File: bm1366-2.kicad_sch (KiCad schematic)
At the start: 73 parts, among them U1 25MHz, U15 TLV3544, U16 AP7331, U17 AP7331, U18 BM1366_mode0, U20 BM1366_mode0

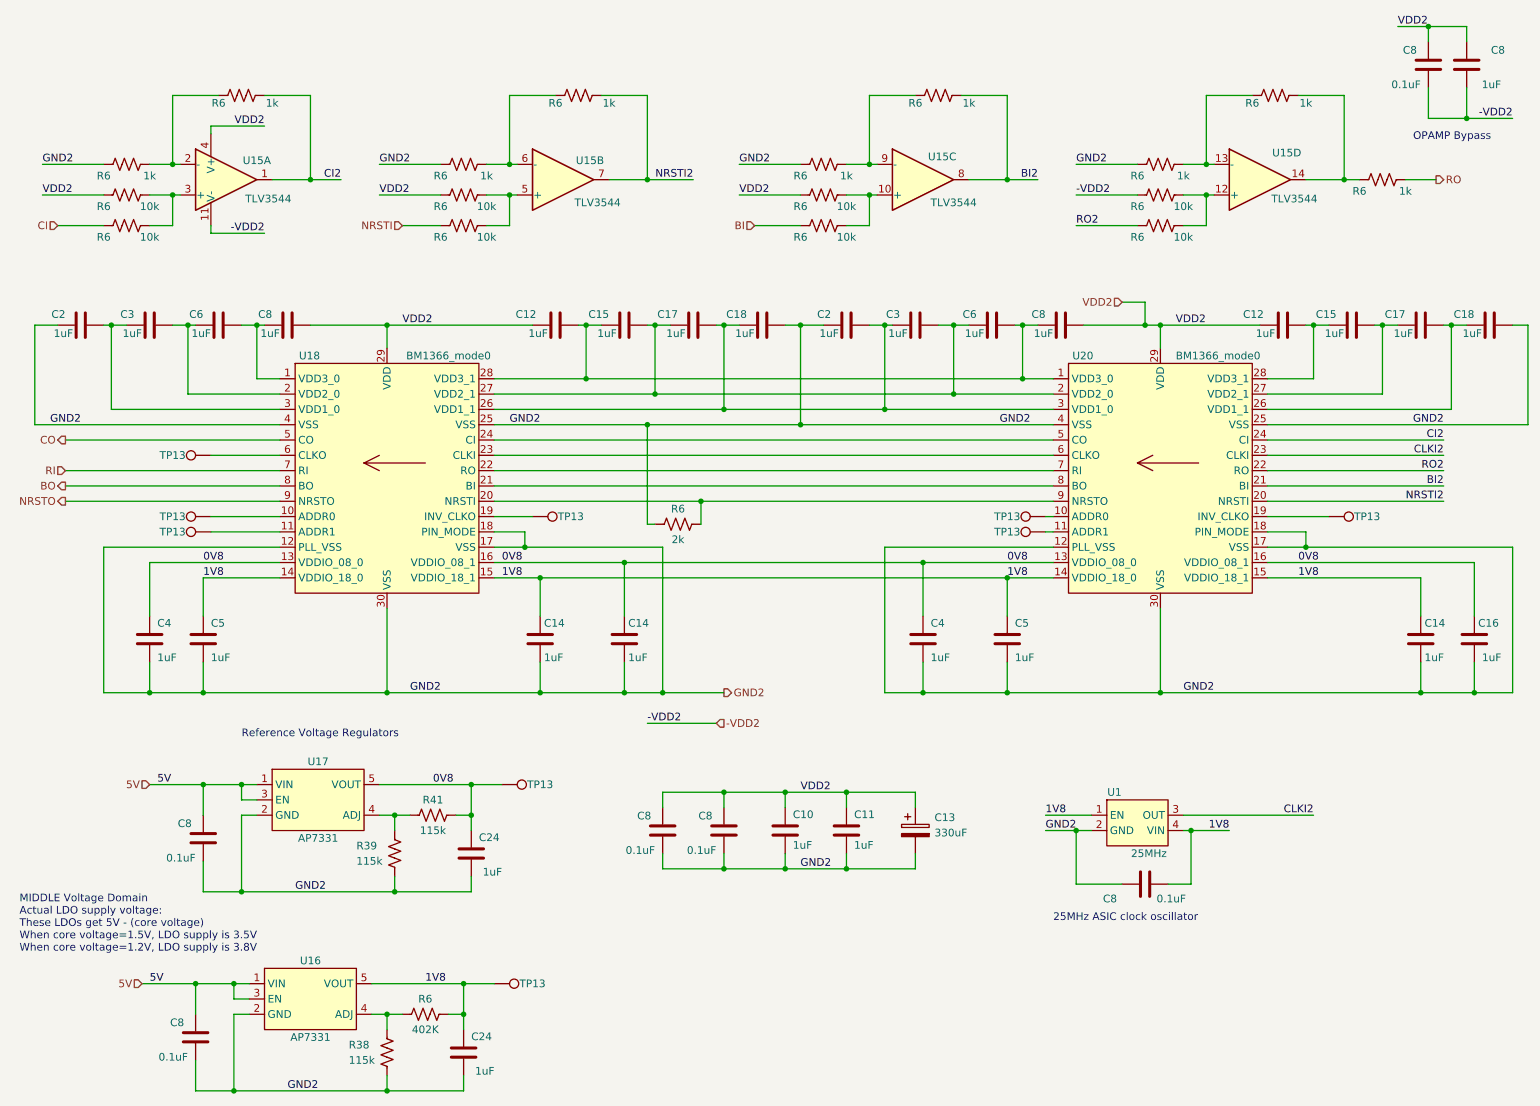
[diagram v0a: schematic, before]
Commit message: finish sch rearrange for BM1368 chain
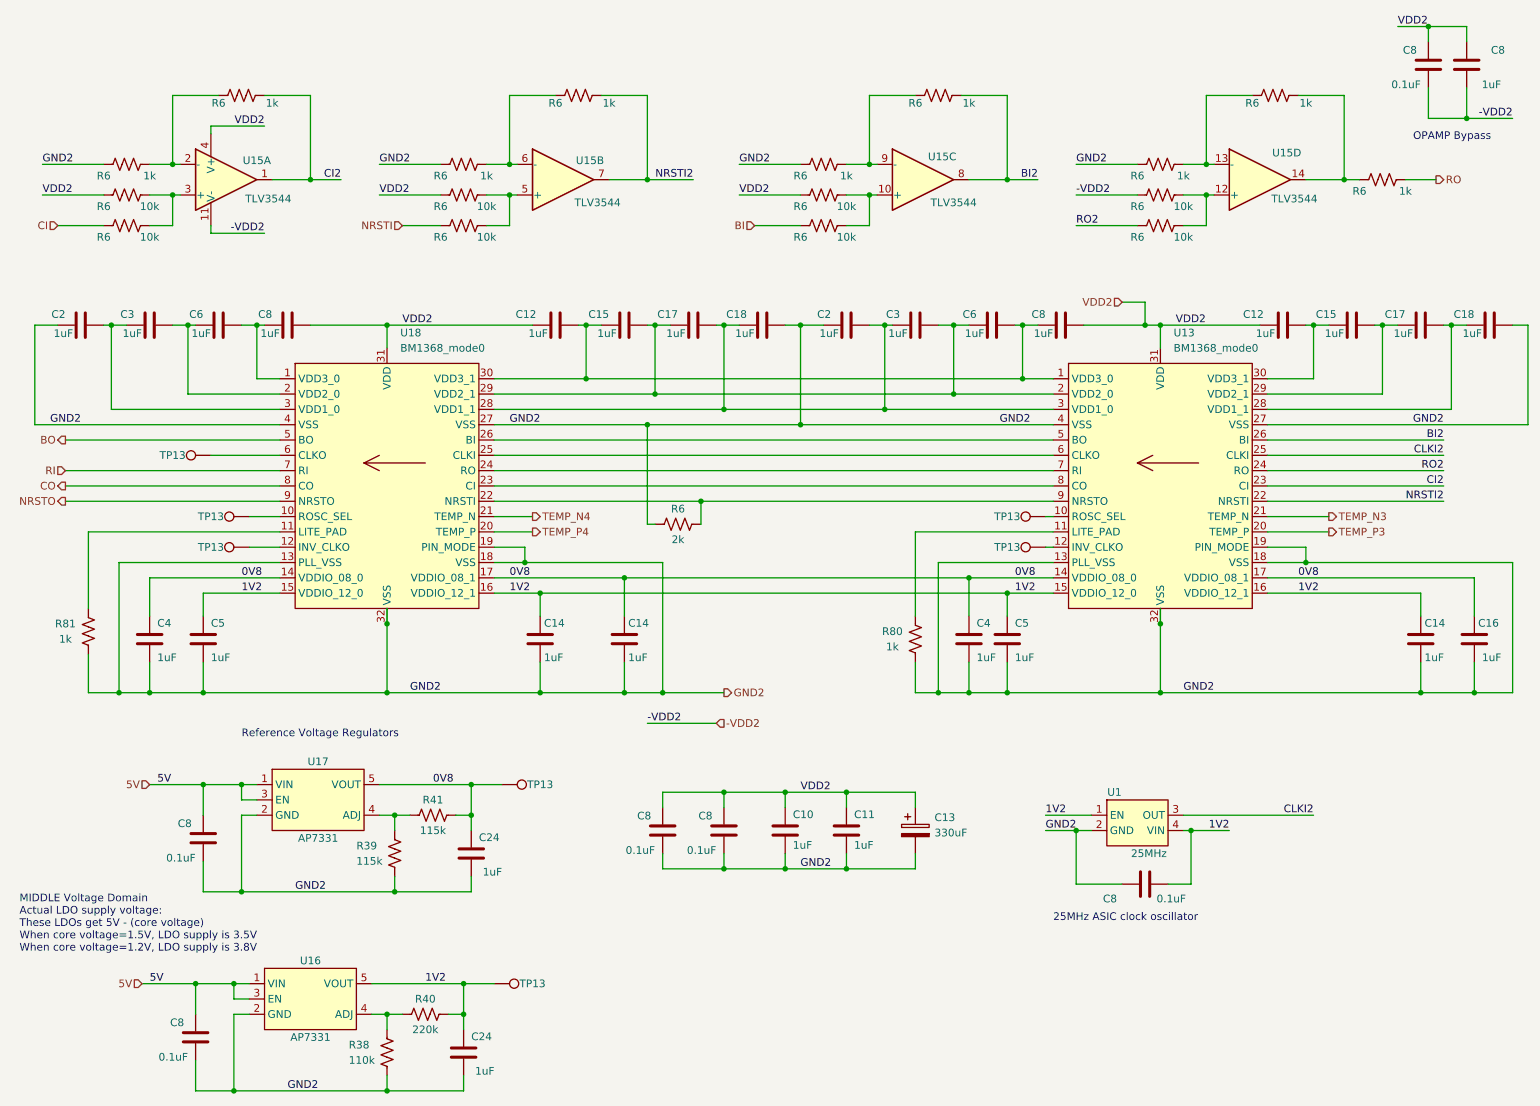
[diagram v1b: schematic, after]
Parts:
- removed R6: 402K, Resistor_SMD:R_0402_1005Metric, symbol Device:R_US
- removed TP13 (x2): TestPoint, TestPoint:TestPoint_Pad_D1.0mm, symbol Connector:TestPoint
- removed U18, U20: BM1366_mode0, bitaxe:BM1366, symbol bitaxe:BM1366_mode0
- added R40: 220k, Resistor_SMD:R_0402_1005Metric, symbol Device:R_US
- added R80, R81: 1k, Resistor_SMD:R_0402_1005Metric, symbol Device:R_US
- added U13, U18: BM1368_mode0, bitaxe:BM1368, symbol bitaxe:BM1368_mode0
- R38: value 115k -> 110k; DK YAG2956CT-ND -> 311-110KLRTR-ND; PARTNO RC0402FR-07115KL -> RC0402FR-07110KL
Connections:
- net 0V8: now also U13.14 (VDDIO_08_0), U13.17 (VDDIO_08_1), U18.14 (VDDIO_08_0), U18.17 (VDDIO_08_1)
- net BI2: now also U13.26 (BI)
- net BO: now also U18.5 (BO)
- net CI2: now also U13.23 (CI)
- net CLKI2: now also U13.25 (CLKI)
- net CO: now also U18.8 (CO)
- net GND2: now also R80.1, R81.1, U13.13 (PLL_VSS), U13.18 (VSS), U13.19 (PIN_MODE), U13.27 (VSS), U13.32 (VSS), U13.4 (VSS), U18.13 (PLL_VSS), U18.18 (VSS), U18.19 (PIN_MODE), U18.27 (VSS), U18.32 (VSS), U18.4 (VSS)
- net NRSTI2: now also U13.22 (NRSTI)
- net NRSTO: now also U18.9 (NRSTO)
- net RI: now also U18.7 (RI)
- net RO2: now also U13.24 (RO)
- net VDD2: now also U13.31 (VDD), U18.31 (VDD)
- net at R6.2: now also U13.9 (NRSTO), U18.22 (NRSTI)
- net at TP13.1: now also U18.10 (ROSC_SEL)
- net at C6.2, C8.1: now also U18.1 (VDD3_0)
- net at C12.2, C15.1, C6.2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: now also U13.1 (VDD3_0), U18.30 (VDD3_1)
- net at C15.2, C17.1, C3.2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: now also U13.2 (VDD2_0), U18.29 (VDD2_1)
- net at TP13.1: now also U18.6 (CLKO)
- net at C17.2, C18.1, C2.2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: now also U13.3 (VDD1_0), U18.28 (VDD1_1)
- net at TP13.1: now also U18.12 (INV_CLKO)
- net at C3.2, C6.1: now also U18.2 (VDD2_0)
- net at C2.2, C3.1: now also U18.3 (VDD1_0)
- net at R38.2, U16.4 (ADJ): now also R40.2
- net at C17.2, C18.1: now also U13.28 (VDD1_1)
- net at TP13.1: now also U13.10 (ROSC_SEL)
- net at TP13.1: now also U13.12 (INV_CLKO)
- net at C12.2, C15.1: now also U13.30 (VDD3_1)
- net at C15.2, C17.1: now also U13.29 (VDD2_1)
- net 1V8 renamed 1V2
- net 1V2: now also R40.1, U13.15 (VDDIO_12_0), U13.16 (VDDIO_12_1), U18.15 (VDDIO_12_0), U18.16 (VDDIO_12_1)
- new net: R80.2, U13.11 (LITE_PAD)
- new net: R81.2, U18.11 (LITE_PAD)
- new net: U13.8 (CO), U18.23 (CI)
- new net: U13.7 (RI), U18.24 (RO)
- new net: U13.6 (CLKO), U18.25 (CLKI)
- new net: U13.5 (BO), U18.26 (BI)
- new net TEMP_N3: U13.21 (TEMP_N)
- new net TEMP_N4: U18.21 (TEMP_N)
- new net TEMP_P3: U13.20 (TEMP_P)
- new net TEMP_P4: U18.20 (TEMP_P)
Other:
- moved on the sheet: C4, TP13

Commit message: Reset to 1V8
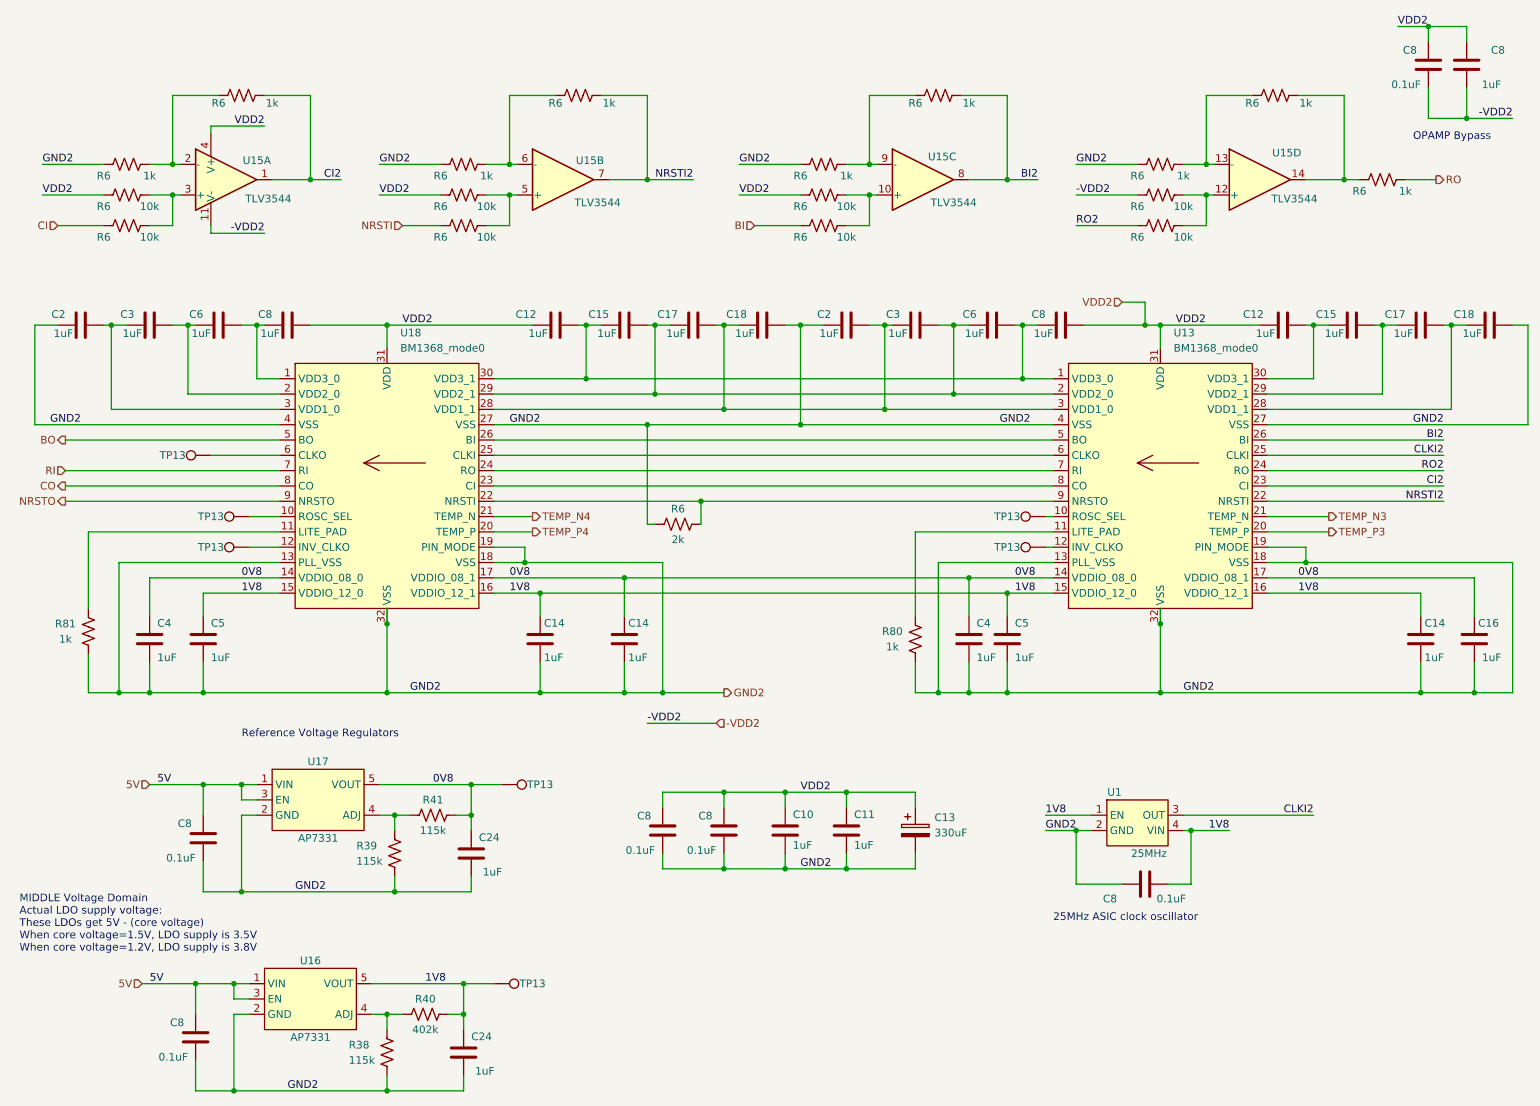
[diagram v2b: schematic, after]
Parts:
- R38: value 110k -> 115k; DK 311-110KLRTR-ND -> YAG2956CT-ND; PARTNO RC0402FR-07110KL -> RC0402FR-07115KL
- R40: value 220k -> 402k; DK 311-220KLRTR-ND -> YAG3151CT-ND; PARTNO RC0402FR-07220KL -> RC0402FR-07402KL
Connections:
- net 1V2 renamed 1V8
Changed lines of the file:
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@@
 		)
 	)
-	(label "1V2"
+	(label "1V8"
 		(at 97.79 111.76 0)
 		(fields_autoplaced yes)
@@
 		)
 	)
-	(label "1V2"
+	(label "1V8"
 		(at 83.82 176.53 0)
 		(fields_autoplaced yes)
@@
 		)
 	)
-	(label "1V2"
+	(label "1V8"
 		(at 217.17 151.13 180)
 		(fields_autoplaced yes)
@@
 		)
 	)
-	(label "1V2"
+	(label "1V8"
 		(at 186.69 148.59 0)
 		(fields_autoplaced yes)
@@
 		)
 	)
-	(label "1V2"
+	(label "1V8"
 		(at 228.6 111.76 0)
 		(fields_autoplaced yes)
@@
 		)
 	)
-	(label "1V2"
+	(label "1V8"
 		(at 53.34 111.76 0)
 		(fields_autoplaced yes)
@@
 		)
 	)
-	(label "1V2"
+	(label "1V8"
 		(at 181.61 111.76 0)
 		(fields_autoplaced yes)
@@
 	)
 	(symbol
+		(lib_id "Device:R_US")
+		(at 77.47 187.96 180)
+		(unit 1)
+		(exclude_from_sim no)
+		(in_bom yes)
+		(on_board yes)
+		(dnp no)
+		(property "Reference" "R38"
+			(at 71.12 186.69 0)
+			(effects
+				(font
+					(size 1.27 1.27)
+				)
+				(justify right)
+			)
+		)
+		(property "Value" "115k"
+			(at 71.12 189.23 0)
+			(effects
+				(font
+					(size 1.27 1.27)
+				)
+				(justify right)
+			)
+		)
+		(property "Footprint" "Resistor_SMD:R_0402_1005Metric"
+			(at 76.454 187.706 90)
+			(effects
+				(font
+					(size 1.27 1.27)
+				)
+				(hide yes)
+			)
+		)
+		(property "Datasheet" "~"
+			(at 77.47 187.96 0)
+			(effects
+				(font
+					(size 1.27 1.27)
+				)
+				(hide yes)
+			)
+		)
+		(property "Description" ""
+			(at 77.47 187.96 0)
+			(effects
+				(font
+					(size 1.27 1.27)
+				)
+				(hide yes)
+			)
+		)
+		(property "DK" "YAG2956CT-ND"
+			(at 77.47 187.96 0)
+			(effects
+				(font
+					(size 1.27 1.27)
+				)
+				(hide yes)
+			)
+		)
+		(property "PARTNO" "RC0402FR-07115KL"
+			(at 77.47 187.96 0)
+			(effects
+				(font
+					(size 1.27 1.27)
+				)
+				(hide yes)
+			)
+		)
+		(pin "1"
+		)
+		(pin "2"
+		)
+		(instances
+			(project "bitaxeHex"
+				(path "/e63e39d7-6ac0-4ffd-8aa3-1841a4541b55/831c2d7c-1b0c-48f0-8d88-f1b4f08c2544"
+					(reference "R38")
+					(unit 1)
+				)
+			)
+		)
+	)
+	(symbol
 		(lib_id "Connector:TestPoint")
 		(at 95.25 176.53 270)
@@
 	(symbol
 		(lib_id "Device:R_US")
+		(at 83.82 181.61 270)
+		(unit 1)
+		(exclude_from_sim no)
+		(in_bom yes)
+		(on_board yes)
+		(dnp no)
+		(property "Reference" "R40"
+			(at 83.82 179.07 90)
+			(effects
+				(font
+					(size 1.27 1.27)
+				)
+			)
+		)
+		(property "Value" "402k"
+			(at 83.82 184.15 90)
+			(effects
+				(font
+					(size 1.27 1.27)
+				)
+			)
+		)
+		(property "Footprint" "Resistor_SMD:R_0402_1005Metric"
+			(at 83.566 182.626 90)
+			(effects
+				(font
+					(size 1.27 1.27)
+				)
+				(hide yes)
+			)
+		)
+		(property "Datasheet" "~"
+			(at 83.82 181.61 0)
+			(effects
+				(font
+					(size 1.27 1.27)
+				)
+				(hide yes)
+			)
+		)
+		(property "Description" ""
+			(at 83.82 181.61 0)
+			(effects
+				(font
+					(size 1.27 1.27)
+				)
+				(hide yes)
+			)
+		)
+		(property "DK" "YAG3151CT-ND"
+			(at 83.82 181.61 0)
+			(effects
+				(font
+					(size 1.27 1.27)
+				)
+				(hide yes)
+			)
+		)
+		(property "PARTNO" "RC0402FR-07402KL"
+			(at 83.82 181.61 0)
+			(effects
+				(font
+					(size 1.27 1.27)
+				)
+				(hide yes)
+			)
+		)
+		(pin "1"
+		)
+		(pin "2"
+		)
+		(instances
+			(project "bitaxeHex"
+				(path "/e63e39d7-6ac0-4ffd-8aa3-1841a4541b55/831c2d7c-1b0c-48f0-8d88-f1b4f08c2544"
+					(reference "R40")
+					(unit 1)
+				)
+			)
+		)
+	)
+	(symbol
+		(lib_id "Device:R_US")
 		(at 149.86 45.72 90)
 		(unit 1)
@@
 	(symbol
 		(lib_id "Device:R_US")
-		(at 77.47 187.96 180)
-		(unit 1)
-		(exclude_from_sim no)
-		(in_bom yes)
-		(on_board yes)
-		(dnp no)
-		(property "Reference" "R38"
-			(at 71.12 186.69 0)
-			(effects
-				(font
-					(size 1.27 1.27)
-				)
-				(justify right)
-			)
-		)
-		(property "Value" "110k"
-			(at 71.12 189.23 0)
-			(effects
-				(font
-					(size 1.27 1.27)
-				)
-				(justify right)
-			)
-		)
-		(property "Footprint" "Resistor_SMD:R_0402_1005Metric"
-			(at 76.454 187.706 90)
-			(effects
-				(font
-					(size 1.27 1.27)
-				)
-				(hide yes)
-			)
-		)
-		(property "Datasheet" "~"
-			(at 77.47 187.96 0)
-			(effects
-				(font
-					(size 1.27 1.27)
-				)
-				(hide yes)
-			)
-		)
-		(property "Description" ""
-			(at 77.47 187.96 0)
-			(effects
-				(font
-					(size 1.27 1.27)
-				)
-				(hide yes)
-			)
-		)
-		(property "DK" "311-110KLRTR-ND"
-			(at 77.47 187.96 0)
-			(effects
-				(font
-					(size 1.27 1.27)
-				)
-				(hide yes)
-			)
-		)
-		(property "PARTNO" "RC0402FR-07110KL"
-			(at 77.47 187.96 0)
-			(effects
-				(font
-					(size 1.27 1.27)
-				)
-				(hide yes)
-			)
-		)
-		(pin "1"
-		)
-		(pin "2"
-		)
-		(instances
-			(project "bitaxeHex"
-				(path "/e63e39d7-6ac0-4ffd-8aa3-1841a4541b55/831c2d7c-1b0c-48f0-8d88-f1b4f08c2544"
-					(reference "R38")
-					(unit 1)
-				)
-			)
-		)
-	)
-	(symbol
-		(lib_id "Device:R_US")
 		(at 242.57 43.18 270)
 		(unit 1)
@@
 					(unit 1)
 				)
-			)
-		)
-	)
-	(symbol
-		(lib_id "Device:R_US")
-		(at 83.82 181.61 270)
-		(unit 1)
-		(exclude_from_sim no)
-		(in_bom yes)
-		(on_board yes)
-		(dnp no)
-		(property "Reference" "R40"
-			(at 83.82 179.07 90)
-			(effects
-				(font
-					(size 1.27 1.27)
-				)
-			)
-		)
-		(property "Value" "220k"
-			(at 83.82 184.15 90)
-			(effects
-				(font
-					(size 1.27 1.27)
-				)
-			)
-		)
-		(property "Footprint" "Resistor_SMD:R_0402_1005Metric"
-			(at 83.566 182.626 90)
-			(effects
-				(font
-					(size 1.27 1.27)
-				)
-				(hide yes)
-			)
-		)
-		(property "Datasheet" "~"
-			(at 83.82 181.61 0)
-			(effects
-				(font
-					(size 1.27 1.27)
-				)
-				(hide yes)
-			)
-		)
-		(property "Description" ""
-			(at 83.82 181.61 0)
-			(effects
-				(font
-					(size 1.27 1.27)
-				)
-				(hide yes)
-			)
-		)
-		(property "DK" "311-220KLRTR-ND"
-			(at 83.82 181.61 0)
-			(effects
-				(font
-					(size 1.27 1.27)
-				)
-				(hide yes)
-			)
-		)
-		(property "PARTNO" "RC0402FR-07220KL"
-			(at 83.82 181.61 0)
-			(effects
-				(font
-					(size 1.27 1.27)
-				)
-				(hide yes)
-			)
-		)
-		(pin "1"
-		)
-		(pin "2"
-		)
-		(instances
-			(project "bitaxeHex"
-				(path "/e63e39d7-6ac0-4ffd-8aa3-1841a4541b55/831c2d7c-1b0c-48f0-8d88-f1b4f08c2544"
-					(reference "R40")
-					(unit 1)
-				)

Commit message: init push for GammaHex
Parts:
- removed U13, U18: BM1368_mode0, bitaxe:BM1368, symbol bitaxe:BM1368_mode0
- added U13, U18: BM1370_mode0, bitaxe:BM1370, symbol bitaxe:BM1370_mode0
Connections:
- net 0V8: now also U13.14 (VDDIO_08_0), U13.17 (VDDIO_08_1), U18.14 (VDDIO_08_0), U18.17 (VDDIO_08_1)
- net 1V8: now also U13.15 (VDDIO_12_0), U13.16 (VDDIO_12_1), U18.15 (VDDIO_12_0), U18.16 (VDDIO_12_1)
- net BI2: now also U18.26 (BI)
- net BO: now also U13.5 (BO)
- net CI2: now also U18.23 (CI)
- net CLKI2: now also U18.25 (CLKI)
- net CO: now also U13.8 (CO)
- net GND2: now also U13.13 (PLL_VSS), U13.18 (VSS), U13.19 (PIN_MODE), U13.27 (VSS), U13.32 (VSS), U13.4 (VSS), U18.13 (PLL_VSS), U18.18 (VSS), U18.19 (PIN_MODE), U18.27 (VSS), U18.32 (VSS), U18.4 (VSS)
- net NRSTI2: now also U18.22 (NRSTI)
- net NRSTO: now also U13.9 (NRSTO)
- net RI: now also U13.7 (RI)
- net RO2: now also U18.24 (RO)
- net TEMP_N3: now also U18.21 (TEMP_N)
- net TEMP_N4: now also U13.21 (TEMP_N)
- net TEMP_P3: now also U18.20 (TEMP_P)
- net TEMP_P4: now also U13.20 (TEMP_P)
- net VDD2: now also U13.31 (VDD), U18.31 (VDD)
- net at R6.2: now also U13.22 (NRSTI), U18.9 (NRSTO)
- net at TP13.1: now also U13.10 (ROSC_SEL)
- net at C6.2, C8.1: now also U13.1 (VDD3_0)
- net at C12.2, C15.1, C6.2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: now also U13.30 (VDD3_1), U18.1 (VDD3_0)
- net at C15.2, C17.1, C3.2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: now also U13.29 (VDD2_1), U18.2 (VDD2_0)
- net at TP13.1: now also U13.6 (CLKO)
- net at C17.2, C18.1, C2.2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: now also U13.28 (VDD1_1), U18.3 (VDD1_0)
- net at C17.2, C18.1: now also U18.28 (VDD1_1)
- net at TP13.1: now also U18.10 (ROSC_SEL)
- net at R80.2: now also U18.11 (LITE_PAD)
- net at TP13.1: now also U18.12 (INV_CLKO)
- net at C12.2, C15.1: now also U18.30 (VDD3_1)
- net at C15.2, C17.1: now also U18.29 (VDD2_1)
- net at C2.2, C3.1: now also U13.3 (VDD1_0)
- net at R81.2: now also U13.11 (LITE_PAD)
- net at TP13.1: now also U13.12 (INV_CLKO)
- net at C3.2, C6.1: now also U13.2 (VDD2_0)
- new net: U13.26 (BI), U18.5 (BO)
- new net: U13.25 (CLKI), U18.6 (CLKO)
- new net: U13.24 (RO), U18.7 (RI)
- new net: U13.23 (CI), U18.8 (CO)
